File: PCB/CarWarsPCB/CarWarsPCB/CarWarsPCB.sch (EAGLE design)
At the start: 11 parts, among them J1 MAGJACK

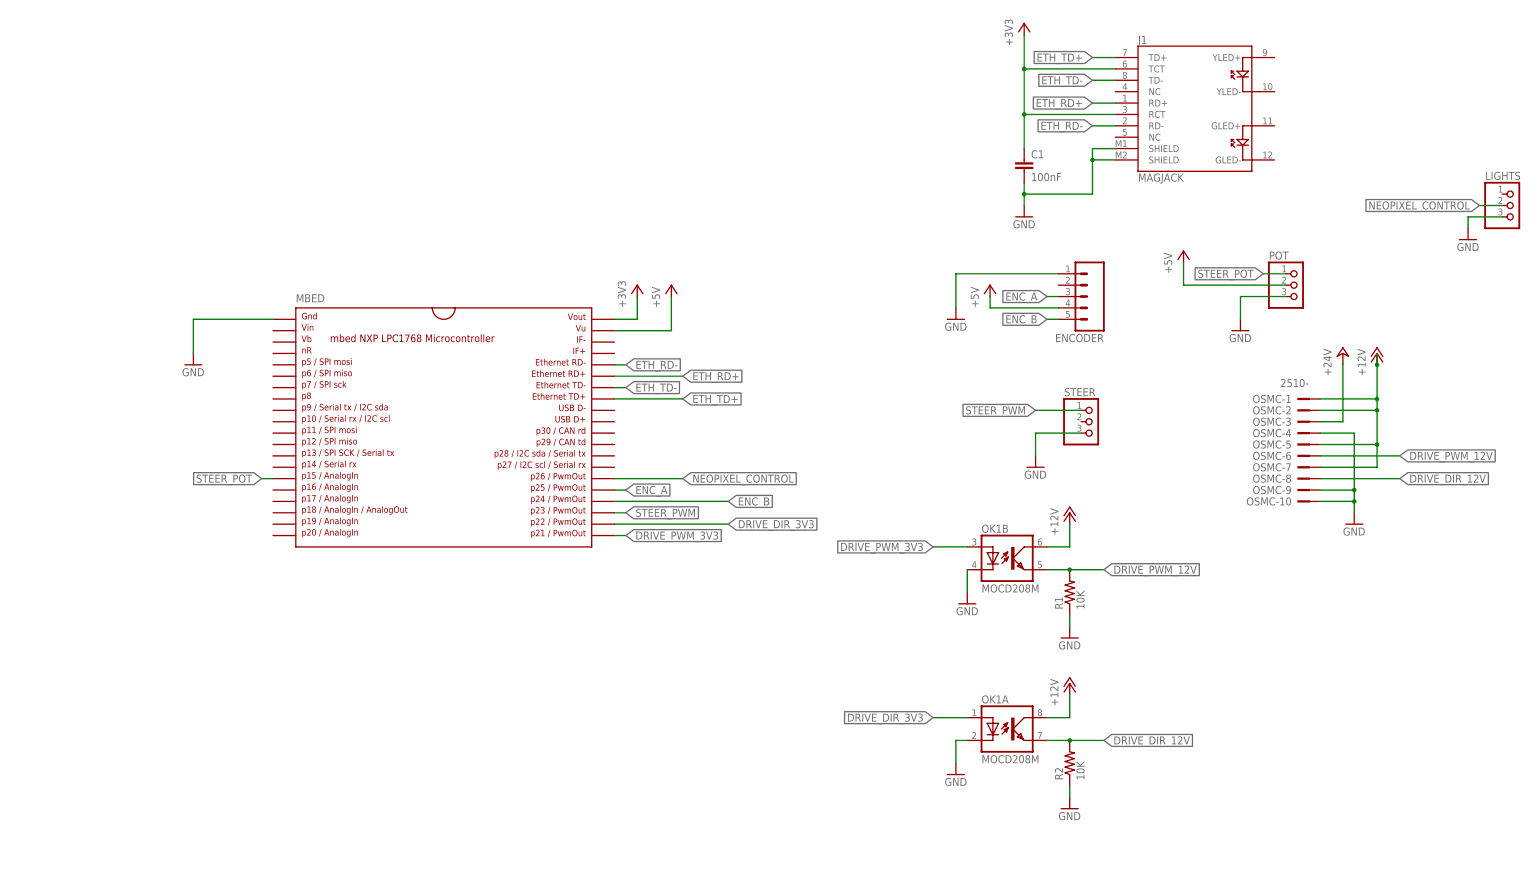
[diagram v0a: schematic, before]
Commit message: Updated CarWars PCB
Adds barrel jack for power
Re-arranges board
Adds e-stop status connector
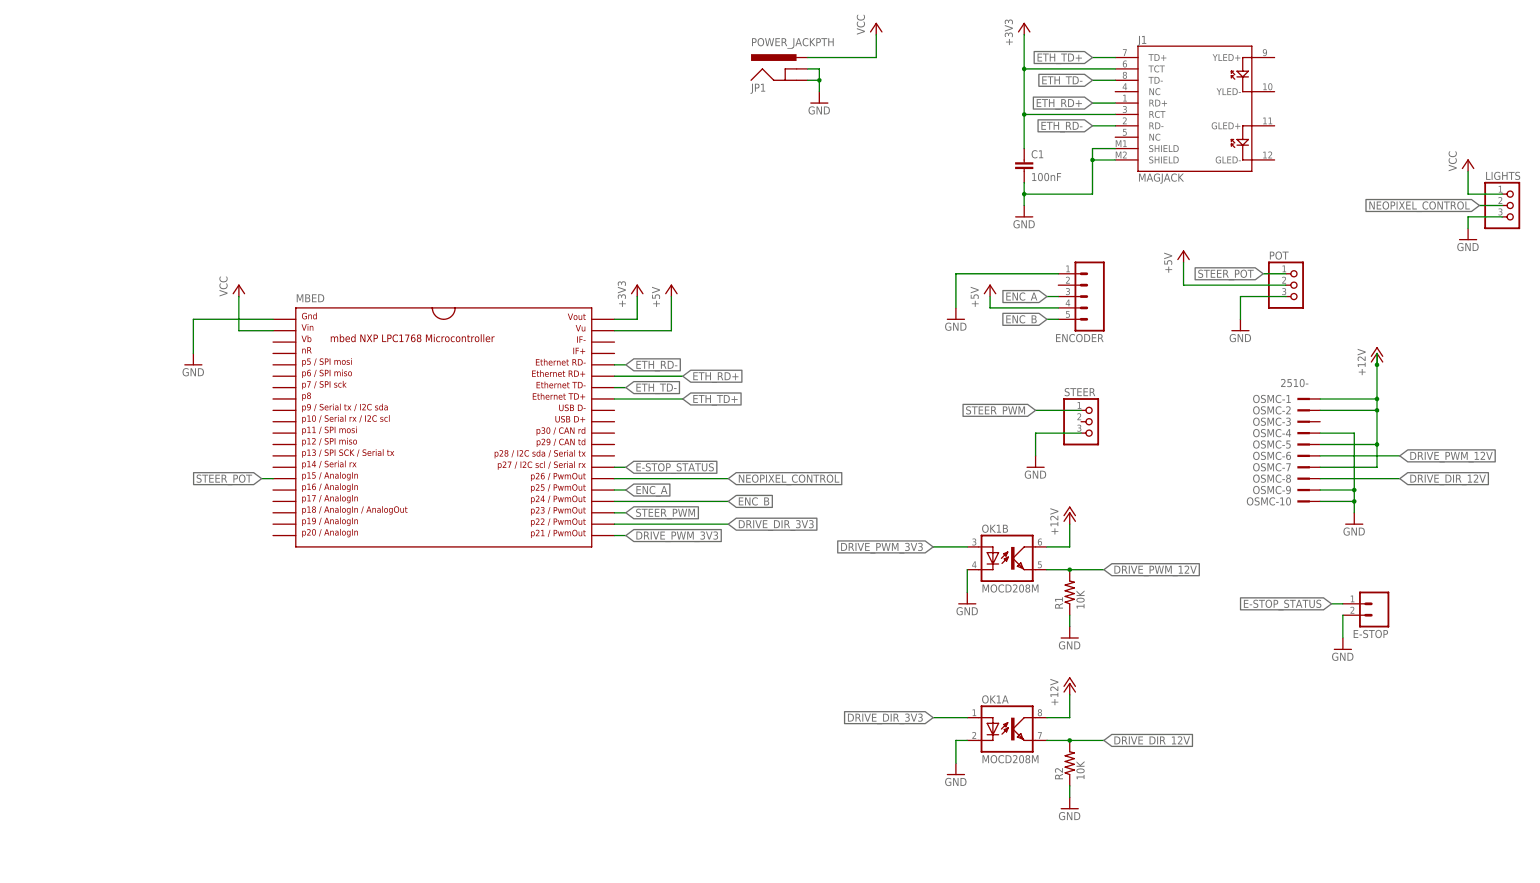
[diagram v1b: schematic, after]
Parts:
- added E-STOP: (no value), SparkFun-Connectors:M02PTH
- added JP1: POWER_JACKPTH, SparkFun-Connectors:POWER_JACKPTH
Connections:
- removed net +24V: OSMC-3.KL
- new net E-STOP_STATUS: E-STOP.1, MBED.P$27
- new net VCC: JP1.PWR, LIGHTS.1, MBED.P$2
- net GND: now also E-STOP.2, JP1.GND, JP1.GNDBREAK
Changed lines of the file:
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@@
 <layer number="115" name="ReferenceISLANDS" color="7" fill="1" visible="yes" active="yes"/>
 <layer number="116" name="Patch_BOT" color="9" fill="4" visible="yes" active="yes"/>
+<layer number="117" name="BACKMAAT1" color="7" fill="1" visible="no" active="no"/>
 <layer number="118" name="Rect_Pads" color="7" fill="1" visible="yes" active="yes"/>
+<layer number="119" name="KAP_TEKEN" color="7" fill="1" visible="no" active="no"/>
+<layer number="120" name="KAP_MAAT1" color="7" fill="1" visible="no" active="no"/>
 <layer number="121" name="_tsilk" color="7" fill="1" visible="yes" active="yes"/>
 <layer number="122" name="_bsilk" color="7" fill="1" visible="yes" active="yes"/>
@@
 <layer number="128" name="_bValues" color="7" fill="1" visible="yes" active="yes"/>
 <layer number="129" name="Mask" color="7" fill="1" visible="yes" active="yes"/>
+<layer number="130" name="SMDSTROOK" color="7" fill="1" visible="no" active="no"/>
 <layer number="131" name="tAdjust" color="7" fill="1" visible="yes" active="yes"/>
 <layer number="132" name="bAdjust" color="7" fill="1" visible="yes" active="yes"/>
+<layer number="133" name="bottom_silk" color="7" fill="1" visible="yes" active="yes"/>
 <layer number="144" name="Drill_legend" color="7" fill="1" visible="yes" active="yes"/>
 <layer number="150" name="Notes" color="7" fill="1" visible="yes" active="yes"/>
@@
 <part name="GND10" library="supply1" library_urn="urn:adsk.eagle:library:371" deviceset="GND" device=""/>
 <part name="P+7" library="supply1" library_urn="urn:adsk.eagle:library:371" deviceset="+12V" device=""/>
-<part name="P+6" library="supply1" library_urn="urn:adsk.eagle:library:371" deviceset="+24V" device=""/>
 <part name="P+4" library="supply1" library_urn="urn:adsk.eagle:library:371" deviceset="+12V" device=""/>
 <part name="P+5" library="supply1" library_urn="urn:adsk.eagle:library:371" deviceset="+12V" device=""/>
 <part name="LIGHTS" library="Roboracing" deviceset="PINHD-1X3" device=""/>
 <part name="GND11" library="supply1" library_urn="urn:adsk.eagle:library:371" deviceset="GND" device=""/>
+<part name="E-STOP" library="SparkFun-Connectors" deviceset="M02" device="PTH"/>
+<part name="GND12" library="supply1" library_urn="urn:adsk.eagle:library:371" deviceset="GND" device=""/>
+<part name="JP1" library="SparkFun-Connectors" deviceset="POWER_JACK" device="PTH"/>
+<part name="GND13" library="supply1" library_urn="urn:adsk.eagle:library:371" deviceset="GND" device=""/>
+<part name="P+10" library="supply1" library_urn="urn:adsk.eagle:library:371" deviceset="VCC" device=""/>
+<part name="P+8" library="supply1" library_urn="urn:adsk.eagle:library:371" deviceset="VCC" device=""/>
+<part name="P+9" library="supply1" library_urn="urn:adsk.eagle:library:371" deviceset="VCC" device=""/>
 </parts>
 <sheets>
@@
 <instance part="GND10" gate="1" x="279.4" y="35.56"/>
 <instance part="P+7" gate="1" x="284.48" y="73.66"/>
-<instance part="P+6" gate="1" x="276.86" y="73.66"/>
 <instance part="P+4" gate="1" x="215.9" y="38.1"/>
 <instance part="P+5" gate="1" x="215.9" y="0"/>
@@
 <instance part="LIGHTS" gate="A" x="314.96" y="106.68"/>
 <instance part="GND11" gate="1" x="304.8" y="99.06"/>
+<instance part="E-STOP" gate="G$1" x="284.48" y="17.78" rot="R180"/>
+<instance part="GND12" gate="1" x="276.86" y="7.62"/>
+<instance part="JP1" gate="G$1" x="154.94" y="132.08" smashed="yes">
+<attribute name="VALUE" x="144.78" y="142.24" size="1.778" layer="96"/>
+<attribute name="NAME" x="144.78" y="132.08" size="1.778" layer="95"/>
+</instance>
+<instance part="GND13" gate="1" x="160.02" y="129.54"/>
+<instance part="P+10" gate="VCC" x="172.72" y="147.32"/>
+<instance part="P+8" gate="VCC" x="304.8" y="116.84"/>
+<instance part="P+9" gate="VCC" x="30.48" y="88.9"/>
 </instances>
 <busses>
@@
 <wire x1="304.8" y1="104.14" x2="304.8" y2="101.6" width="0.1524" layer="91"/>
 <pinref part="GND11" gate="1" pin="GND"/>
+</segment>
+<segment>
+<pinref part="GND12" gate="1" pin="GND"/>
+<pinref part="E-STOP" gate="G$1" pin="2"/>
+<wire x1="276.86" y1="10.16" x2="276.86" y2="15.24" width="0.1524" layer="91"/>
+</segment>
+<segment>
+<pinref part="JP1" gate="G$1" pin="GND"/>
+<wire x1="157.48" y1="134.62" x2="160.02" y2="134.62" width="0.1524" layer="91"/>
+<wire x1="160.02" y1="134.62" x2="160.02" y2="132.08" width="0.1524" layer="91"/>
+<pinref part="JP1" gate="G$1" pin="GNDBREAK"/>
+<wire x1="157.48" y1="137.16" x2="160.02" y2="137.16" width="0.1524" layer="91"/>
+<wire x1="160.02" y1="137.16" x2="160.02" y2="134.62" width="0.1524" layer="91"/>
+<junction x="160.02" y="134.62"/>
+<pinref part="GND13" gate="1" pin="GND"/>
 </segment>
 </net>
@@
 </segment>
 </net>
-<net name="+24V" class="0">
-<segment>
-<pinref part="OSMC" gate="-3" pin="KL"/>
-<pinref part="P+6" gate="1" pin="+24V"/>
-<wire x1="271.78" y1="58.42" x2="276.86" y2="58.42" width="0.1524" layer="91"/>
-<wire x1="276.86" y1="58.42" x2="276.86" y2="71.12" width="0.1524" layer="91"/>
-</segment>
-</net>
 <net name="NEOPIXEL_CONTROL" class="0">
 <segment>
@@
 <segment>
 <pinref part="MBED" gate="G$1" pin="P$26"/>
-<wire x1="114.3" y1="45.72" x2="129.54" y2="45.72" width="0.1524" layer="91"/>
-<label x="129.54" y="45.72" size="1.778" layer="95" xref="yes"/>
+<wire x1="114.3" y1="45.72" x2="139.7" y2="45.72" width="0.1524" layer="91"/>
+<label x="139.7" y="45.72" size="1.778" layer="95" xref="yes"/>
+</segment>
+</net>
+<net name="E-STOP_STATUS" class="0">
+<segment>
+<pinref part="MBED" gate="G$1" pin="P$27"/>
+<wire x1="114.3" y1="48.26" x2="116.84" y2="48.26" width="0.1524" layer="91"/>
+<label x="116.84" y="48.26" size="1.778" layer="95" xref="yes"/>
+</segment>
+<segment>
+<pinref part="E-STOP" gate="G$1" pin="1"/>
+<wire x1="276.86" y1="17.78" x2="274.32" y2="17.78" width="0.1524" layer="91"/>
+<label x="274.32" y="17.78" size="1.778" layer="95" rot="R180" xref="yes"/>
+</segment>
+</net>
+<net name="VCC" class="0">
+<segment>
+<pinref part="JP1" gate="G$1" pin="PWR"/>
+<wire x1="157.48" y1="139.7" x2="172.72" y2="139.7" width="0.1524" layer="91"/>
+<wire x1="172.72" y1="139.7" x2="172.72" y2="144.78" width="0.1524" layer="91"/>
+<pinref part="P+10" gate="VCC" pin="VCC"/>
+</segment>
+<segment>
+<pinref part="LIGHTS" gate="A" pin="1"/>
+<pinref part="P+8" gate="VCC" pin="VCC"/>
+<wire x1="312.42" y1="109.22" x2="304.8" y2="109.22" width="0.1524" layer="91"/>
+<wire x1="304.8" y1="109.22" x2="304.8" y2="114.3" width="0.1524" layer="91"/>
+</segment>
+<segment>
+<pinref part="P+9" gate="VCC" pin="VCC"/>
+<pinref part="MBED" gate="G$1" pin="P$2"/>
+<wire x1="30.48" y1="86.36" x2="30.48" y2="78.74" width="0.1524" layer="91"/>
+<wire x1="30.48" y1="78.74" x2="38.1" y2="78.74" width="0.1524" layer="91"/>
 </segment>
 </net>
@@
 </sheet>
 </sheets>
+<errors>
+</errors>
 </schematic>
 </drawing>

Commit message: Updates CarWars PCB
Adds connector for SprkFun Current/Voltage sensor
Adds mounting holes to board layout
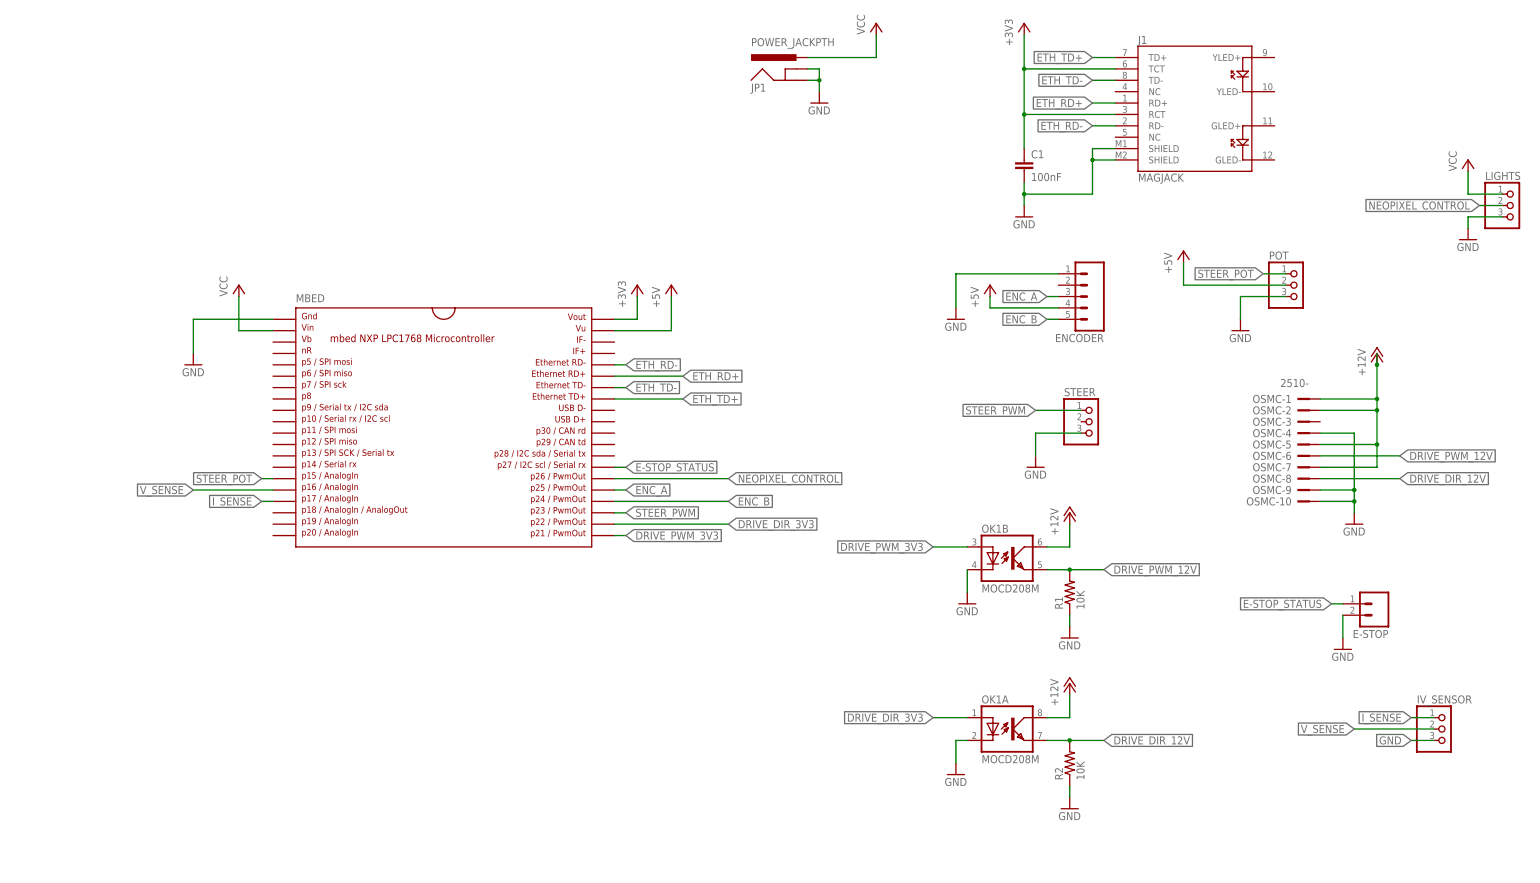
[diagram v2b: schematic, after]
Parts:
- added IV_SENSOR: (no value), Roboracing:PINHD-1X3
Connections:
- new net I_SENSE: IV_SENSOR.1, MBED.P$17
- new net V_SENSE: IV_SENSOR.2, MBED.P$16
- net GND: now also IV_SENSOR.3
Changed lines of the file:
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@@
 <part name="P+8" library="supply1" library_urn="urn:adsk.eagle:library:371" deviceset="VCC" device=""/>
 <part name="P+9" library="supply1" library_urn="urn:adsk.eagle:library:371" deviceset="VCC" device=""/>
+<part name="IV_SENSOR" library="Roboracing" deviceset="PINHD-1X3" device=""/>
 </parts>
 <sheets>
@@
 <instance part="P+8" gate="VCC" x="304.8" y="116.84"/>
 <instance part="P+9" gate="VCC" x="30.48" y="88.9"/>
+<instance part="IV_SENSOR" gate="A" x="299.72" y="-10.16"/>
 </instances>
 <busses>
@@
 <junction x="160.02" y="134.62"/>
 <pinref part="GND13" gate="1" pin="GND"/>
+</segment>
+<segment>
+<pinref part="IV_SENSOR" gate="A" pin="3"/>
+<wire x1="297.18" y1="-12.7" x2="292.1" y2="-12.7" width="0.1524" layer="91"/>
+<label x="292.1" y="-12.7" size="1.778" layer="95" rot="R180" xref="yes"/>
 </segment>
 </net>
@@
 </segment>
 </net>
+<net name="I_SENSE" class="0">
+<segment>
+<pinref part="IV_SENSOR" gate="A" pin="1"/>
+<wire x1="297.18" y1="-7.62" x2="292.1" y2="-7.62" width="0.1524" layer="91"/>
+<label x="292.1" y="-7.62" size="1.778" layer="95" rot="R180" xref="yes"/>
+</segment>
+<segment>
+<pinref part="MBED" gate="G$1" pin="P$17"/>
+<wire x1="38.1" y1="40.64" x2="35.56" y2="40.64" width="0.1524" layer="91"/>
+<label x="35.56" y="40.64" size="1.778" layer="95" rot="R180" xref="yes"/>
+</segment>
+</net>
+<net name="V_SENSE" class="0">
+<segment>
+<pinref part="IV_SENSOR" gate="A" pin="2"/>
+<wire x1="297.18" y1="-10.16" x2="279.4" y2="-10.16" width="0.1524" layer="91"/>
+<label x="279.4" y="-10.16" size="1.778" layer="95" rot="R180" xref="yes"/>
+</segment>
+<segment>
+<pinref part="MBED" gate="G$1" pin="P$16"/>
+<wire x1="38.1" y1="43.18" x2="20.32" y2="43.18" width="0.1524" layer="91"/>
+<label x="20.32" y="43.18" size="1.778" layer="95" rot="R180" xref="yes"/>
+</segment>
+</net>
